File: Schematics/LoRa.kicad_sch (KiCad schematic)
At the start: 2 parts, among them J7 Conn_Coaxial_Small, U5 RFM95W-915S2

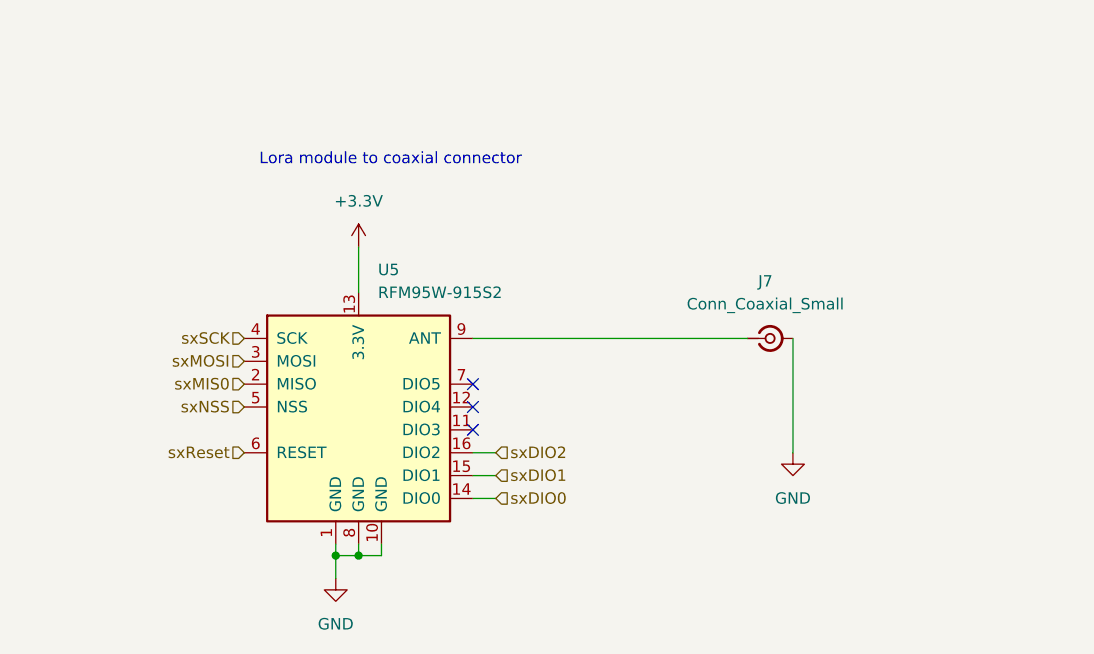
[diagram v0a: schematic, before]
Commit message: reviewed schematic and pcb and replaced part numbers, added and named datasheets into document folder
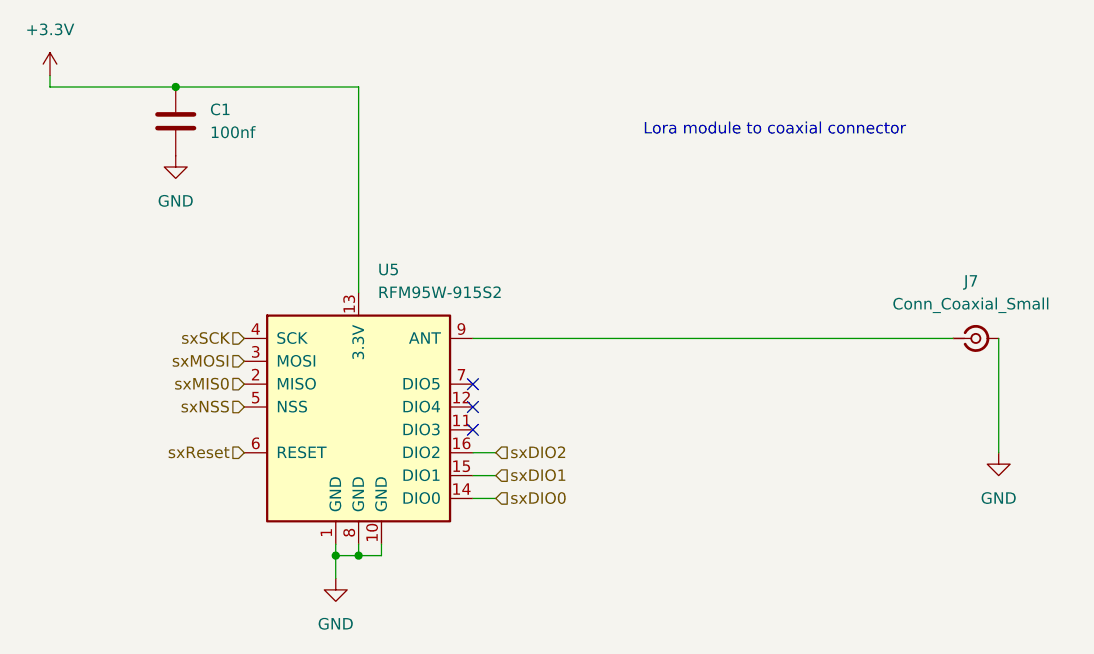
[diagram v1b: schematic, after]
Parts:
- added C1: 100nf, Capacitor_SMD:C_0805_2012Metric_Pad1.18x1.45mm_HandSolder, symbol Device:C
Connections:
- net +3.3V: now also C1.1
- net GND: now also C1.2
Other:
- moved on the sheet: J7
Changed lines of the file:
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@@
 	(text "Lora module to coaxial connector"
 		(exclude_from_sim no)
-		(at 134.366 56.388 0)
+		(at 177.038 53.086 0)
 		(effects
 			(font
@@
 	)
 	(junction
+		(at 110.49 48.26)
+		(diameter 0)
+		(color 0 0 0 0)
+	)
+	(junction
 		(at 130.81 100.33)
 		(diameter 0)
@@
 	(wire
 		(pts
+			(xy 130.81 48.26) (xy 130.81 71.12)
+		)
+		(stroke
+			(width 0)
+			(type default)
+		)
+	)
+	(wire
+		(pts
+			(xy 110.49 48.26) (xy 130.81 48.26)
+		)
+		(stroke
+			(width 0)
+			(type default)
+		)
+	)
+	(wire
+		(pts
 			(xy 130.81 100.33) (xy 128.27 100.33)
 		)
@@
 	(wire
 		(pts
-			(xy 179.07 88.9) (xy 179.07 76.2)
+			(xy 201.93 88.9) (xy 201.93 76.2)
+		)
+		(stroke
+			(width 0)
+			(type default)
+		)
+	)
+	(wire
+		(pts
+			(xy 96.52 48.26) (xy 110.49 48.26)
 		)
 		(stroke
@@
 	(wire
 		(pts
-			(xy 173.99 76.2) (xy 143.51 76.2)
+			(xy 196.85 76.2) (xy 143.51 76.2)
 		)
 		(stroke
@@
 	(wire
 		(pts
-			(xy 130.81 66.04) (xy 130.81 71.12)
+			(xy 96.52 46.99) (xy 96.52 48.26)
 		)
 		(stroke
@@
 	)
 	(symbol
+		(lib_id "power:GND")
+		(at 110.49 55.88 0)
+		(unit 1)
+		(exclude_from_sim no)
+		(in_bom yes)
+		(on_board yes)
+		(dnp no)
+		(fields_autoplaced yes)
+		(property "Reference" "#PWR067"
+			(at 110.49 62.23 0)
+			(effects
+				(font
+					(size 1.27 1.27)
+				)
+				(hide yes)
+			)
+		)
+		(property "Value" "GND"
+			(at 110.49 60.96 0)
+			(effects
+				(font
+					(size 1.27 1.27)
+				)
+			)
+		)
+		(property "Footprint" ""
+			(at 110.49 55.88 0)
+			(effects
+				(font
+					(size 1.27 1.27)
+				)
+				(hide yes)
+			)
+		)
+		(property "Datasheet" ""
+			(at 110.49 55.88 0)
+			(effects
+				(font
+					(size 1.27 1.27)
+				)
+				(hide yes)
+			)
+		)
+		(property "Description" "Power symbol creates a global label with name \"GND\" , ground"
+			(at 110.49 55.88 0)
+			(effects
+				(font
+					(size 1.27 1.27)
+				)
+				(hide yes)
+			)
+		)
+		(pin "1"
+		)
+		(instances
+			(project "flightcomputer2"
+				(path "/6cb3dda3-5fe8-4715-b831-354360aa3199/97ae08f8-7044-40a2-9385-378b47d6b9a1"
+					(reference "#PWR067")
+					(unit 1)
+				)
+			)
+		)
+	)
+	(symbol
 		(lib_id "power:+3.3V")
-		(at 130.81 66.04 0)
+		(at 96.52 46.99 0)
 		(unit 1)
 		(exclude_from_sim no)
@@
 		(fields_autoplaced yes)
 		(property "Reference" "#PWR065"
-			(at 130.81 69.85 0)
+			(at 96.52 50.8 0)
 			(effects
 				(font
@@
 		)
 		(property "Value" "+3.3V"
-			(at 130.81 60.96 0)
+			(at 96.52 41.91 0)
 			(effects
 				(font
@@
 		)
 		(property "Footprint" ""
-			(at 130.81 66.04 0)
+			(at 96.52 46.99 0)
 			(effects
 				(font
@@
 		)
 		(property "Datasheet" ""
-			(at 130.81 66.04 0)
+			(at 96.52 46.99 0)
 			(effects
 				(font
@@
 		)
 		(property "Description" "Power symbol creates a global label with name \"+3.3V\""
-			(at 130.81 66.04 0)
+			(at 96.52 46.99 0)
 			(effects
 				(font
@@
 	(symbol
 		(lib_id "Connector:Conn_Coaxial_Small")
-		(at 176.53 76.2 0)
+		(at 199.39 76.2 0)
 		(unit 1)
 		(exclude_from_sim no)
@@
 		(fields_autoplaced yes)
 		(property "Reference" "J7"
-			(at 176.0104 69.85 0)
+			(at 198.8704 69.85 0)
 			(effects
 				(font
@@
 		)
 		(property "Value" "Conn_Coaxial_Small"
-			(at 176.0104 72.39 0)
+			(at 198.8704 72.39 0)
 			(effects
 				(font
@@
 		)
 		(property "Footprint" "Connector_Coaxial:SMA_Amphenol_132291_Vertical"
-			(at 176.53 76.2 0)
+			(at 199.39 76.2 0)
 			(effects
 				(font
@@
 		)
 		(property "Datasheet" "~"
-			(at 176.53 76.2 0)
+			(at 199.39 76.2 0)
 			(effects
 				(font
@@
 		)
 		(property "Description" "small coaxial connector (BNC, SMA, SMB, SMC, Cinch/RCA, LEMO, ...)"
-			(at 176.53 76.2 0)
+			(at 199.39 76.2 0)
 			(effects
 				(font
@@
 		)
 		(property "Description_1" ""
-			(at 176.53 76.2 0)
+			(at 199.39 76.2 0)
 			(effects
 				(font
@@
 		)
 		(property "MF" ""
-			(at 176.53 76.2 0)
+			(at 199.39 76.2 0)
 			(effects
 				(font
@@
 		)
 		(property "MP" ""
-			(at 176.53 76.2 0)
+			(at 199.39 76.2 0)
 			(effects
 				(font
@@
 		)
 		(property "Package" ""
-			(at 176.53 76.2 0)
+			(at 199.39 76.2 0)
 			(effects
 				(font
@@
 		)
 		(property "Price" ""
-			(at 176.53 76.2 0)
+			(at 199.39 76.2 0)
 			(effects
 				(font
@@
 		)
 		(property "Purchase-URL" ""
-			(at 176.53 76.2 0)
+			(at 199.39 76.2 0)
 			(effects
 				(font
@@
 		)
 		(property "LCSC" "C3172376"
-			(at 176.53 76.2 0)
+			(at 199.39 76.2 0)
 			(effects
 				(font
@@
 		)
 		(property "MANUFACTURER" ""
-			(at 176.53 76.2 0)
+			(at 199.39 76.2 0)
 			(effects
 				(font
@@
 		)
 		(property "MAXIMUM_PACKAGE_HEIGHT" ""
-			(at 176.53 76.2 0)
+			(at 199.39 76.2 0)
 			(effects
 				(font
@@
 		)
 		(property "PARTREV" ""
-			(at 176.53 76.2 0)
+			(at 199.39 76.2 0)
 			(effects
 				(font
@@
 		)
 		(property "STANDARD" ""
-			(at 176.53 76.2 0)
+			(at 199.39 76.2 0)
 			(effects
 				(font
@@
 	(symbol
 		(lib_id "power:GND")
-		(at 179.07 88.9 0)
+		(at 201.93 88.9 0)
 		(unit 1)
 		(exclude_from_sim no)
@@
 		(fields_autoplaced yes)
 		(property "Reference" "#PWR066"
-			(at 179.07 95.25 0)
+			(at 201.93 95.25 0)
 			(effects
 				(font
@@
 		)
 		(property "Value" "GND"
-			(at 179.07 93.98 0)
+			(at 201.93 93.98 0)
 			(effects
 				(font
@@
 		)
 		(property "Footprint" ""
-			(at 179.07 88.9 0)
+			(at 201.93 88.9 0)
 			(effects
 				(font
@@
 		)
 		(property "Datasheet" ""
-			(at 179.07 88.9 0)
+			(at 201.93 88.9 0)
 			(effects
 				(font
@@
 		)
 		(property "Description" "Power symbol creates a global label with name \"GND\" , ground"
-			(at 179.07 88.9 0)
+			(at 201.93 88.9 0)
 			(effects
 				(font
@@
 					(unit 1)
 				)
+			)
+		)
+	)
+	(symbol
+		(lib_id "Device:C")
+		(at 110.49 52.07 0)
+		(unit 1)
+		(exclude_from_sim no)
+		(in_bom yes)
+		(on_board yes)
+		(dnp no)
+		(fields_autoplaced yes)
+		(property "Reference" "C1"
+			(at 114.3 50.7999 0)
+			(effects
+				(font
+					(size 1.27 1.27)
+				)
+				(justify left)
+			)
+		)
+		(property "Value" "100nf"
+			(at 114.3 53.3399 0)
+			(effects
+				(font
+					(size 1.27 1.27)
+				)
+				(justify left)
+			)
+		)
+		(property "Footprint" "Capacitor_SMD:C_0805_2012Metric_Pad1.18x1.45mm_HandSolder"
+			(at 111.4552 55.88 0)
+			(effects
+				(font
+					(size 1.27 1.27)
+				)
+				(hide yes)
+			)
+		)
+		(property "Datasheet" "~"
+			(at 110.49 52.07 0)
+			(effects
+				(font
+					(size 1.27 1.27)
+				)
+				(hide yes)
+			)
+		)
+		(property "Description" "Unpolarized capacitor"
+			(at 110.49 52.07 0)
+			(effects
+				(font
+					(size 1.27 1.27)
+				)
+				(hide yes)
+			)
+		)
+		(pin "2"
+		)
+		(pin "1"
+		)
+		(instances
+			(project ""
+				(path "/6cb3dda3-5fe8-4715-b831-354360aa3199/97ae08f8-7044-40a2-9385-378b47d6b9a1"
+					(reference "C1")
+					(unit 1)
+				)

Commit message: updated to KiCad 10.0, updated .gitignore
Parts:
- C1: LCSC (none) -> C49678
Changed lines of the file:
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@@
+			)
+		)
+		(property "LCSC" "C49678"
+			(at 110.49 52.07 0)
+			(effects
+				(font
+					(size 1.27 1.27)
+				)
+				(hide yes)
 			)
 		)
